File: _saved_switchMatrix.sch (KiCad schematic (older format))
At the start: 54 parts, among them J19 Mono_AudioConnector, J20 Mono_AudioConnector, J21 Mono_AudioConnector, J22 Mono_AudioConnector

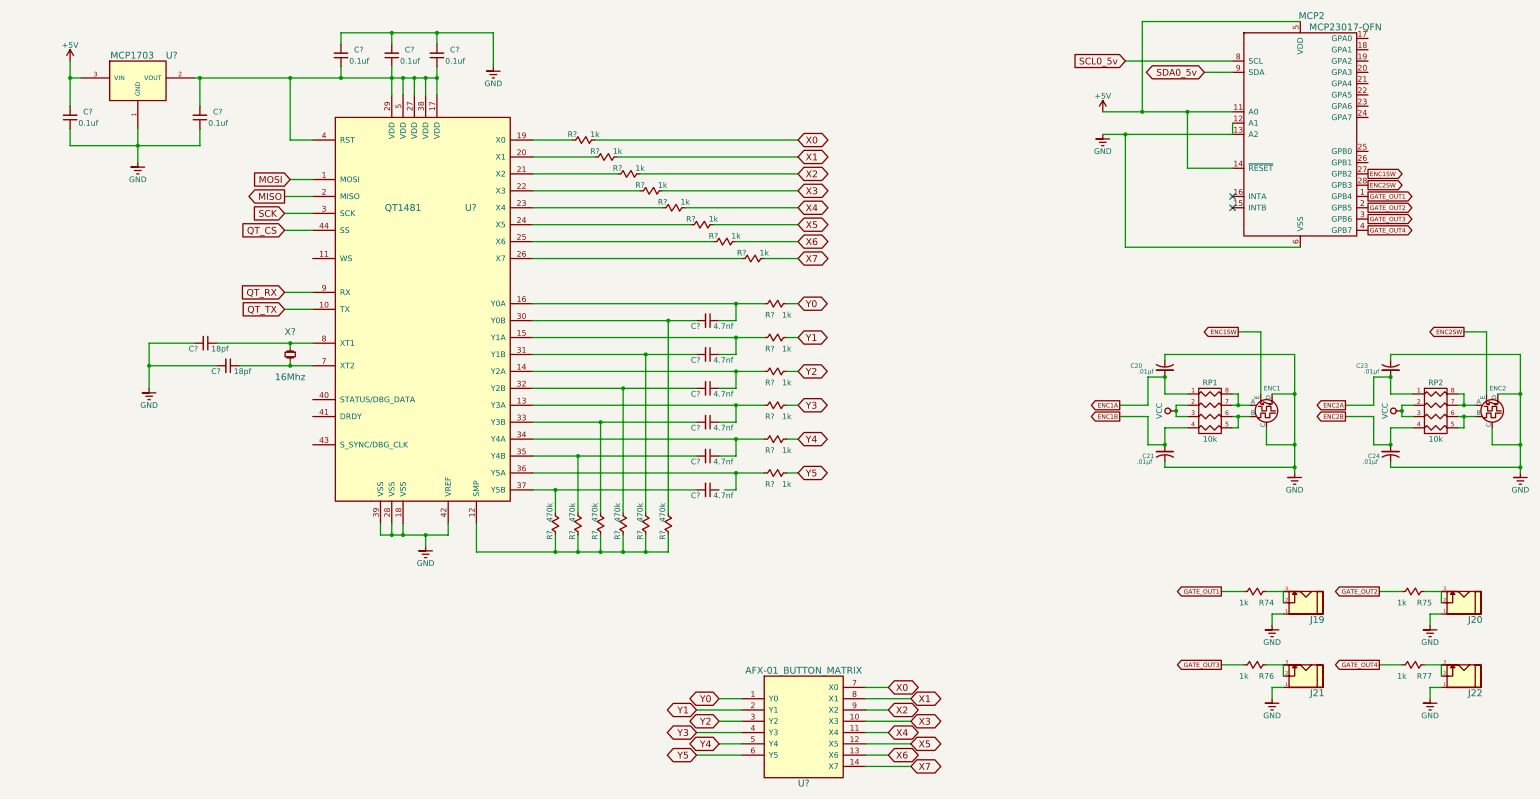
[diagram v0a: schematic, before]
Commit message: Added Touch Capacitive Panel
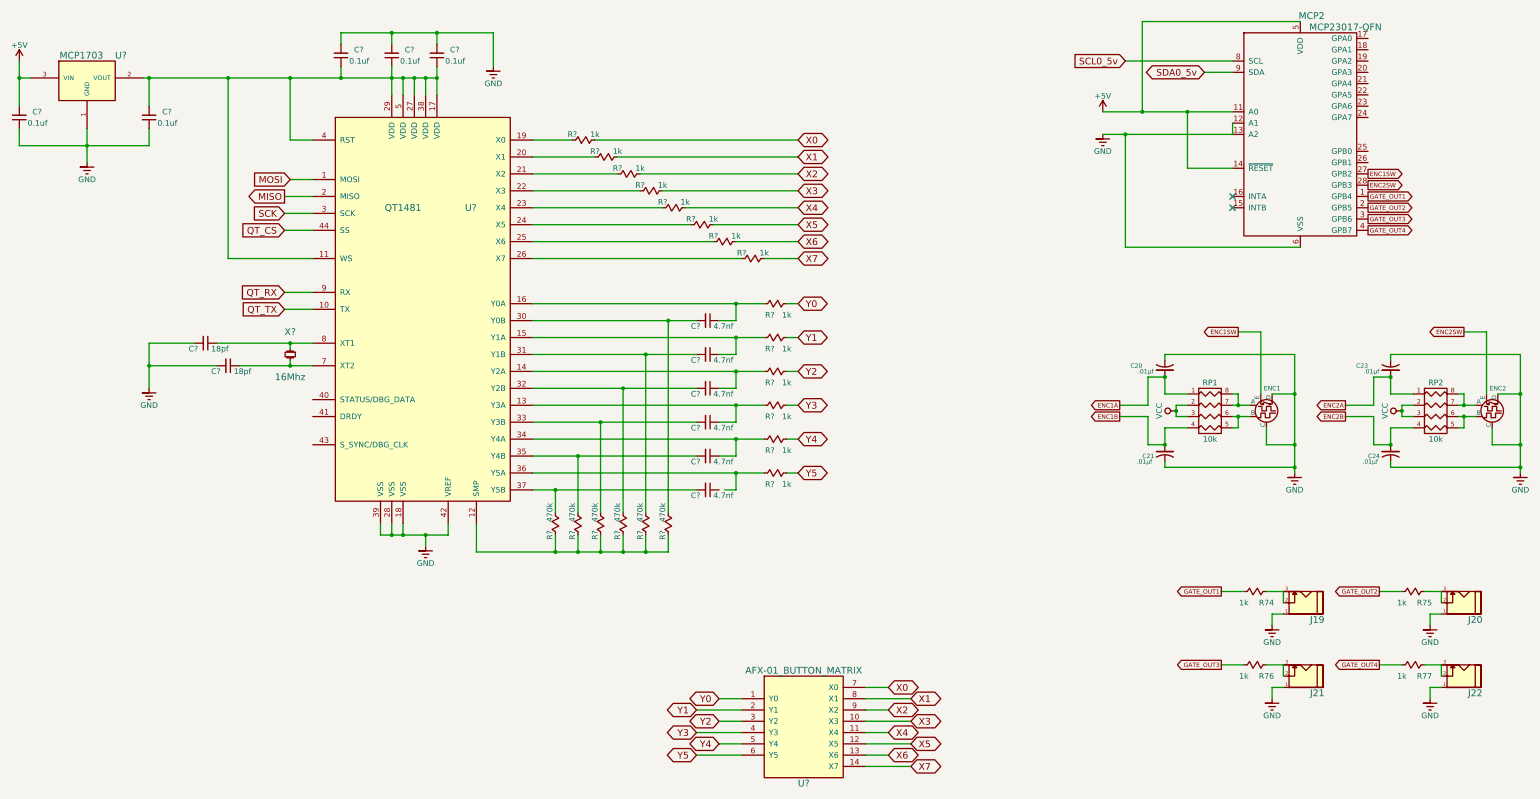
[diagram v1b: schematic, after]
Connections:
- net at U?.11 (WS): now also C?.1, C?.1, C?.1, C?.2, U?.17 (VDD), U?.2 (VOUT), U?.27 (VDD), U?.29 (VDD), U?.38 (VDD), U?.4 (RST), U?.5 (VDD)
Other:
- moved on the sheet: C?, U?
